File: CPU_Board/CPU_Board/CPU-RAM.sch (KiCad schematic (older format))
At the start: 65 parts

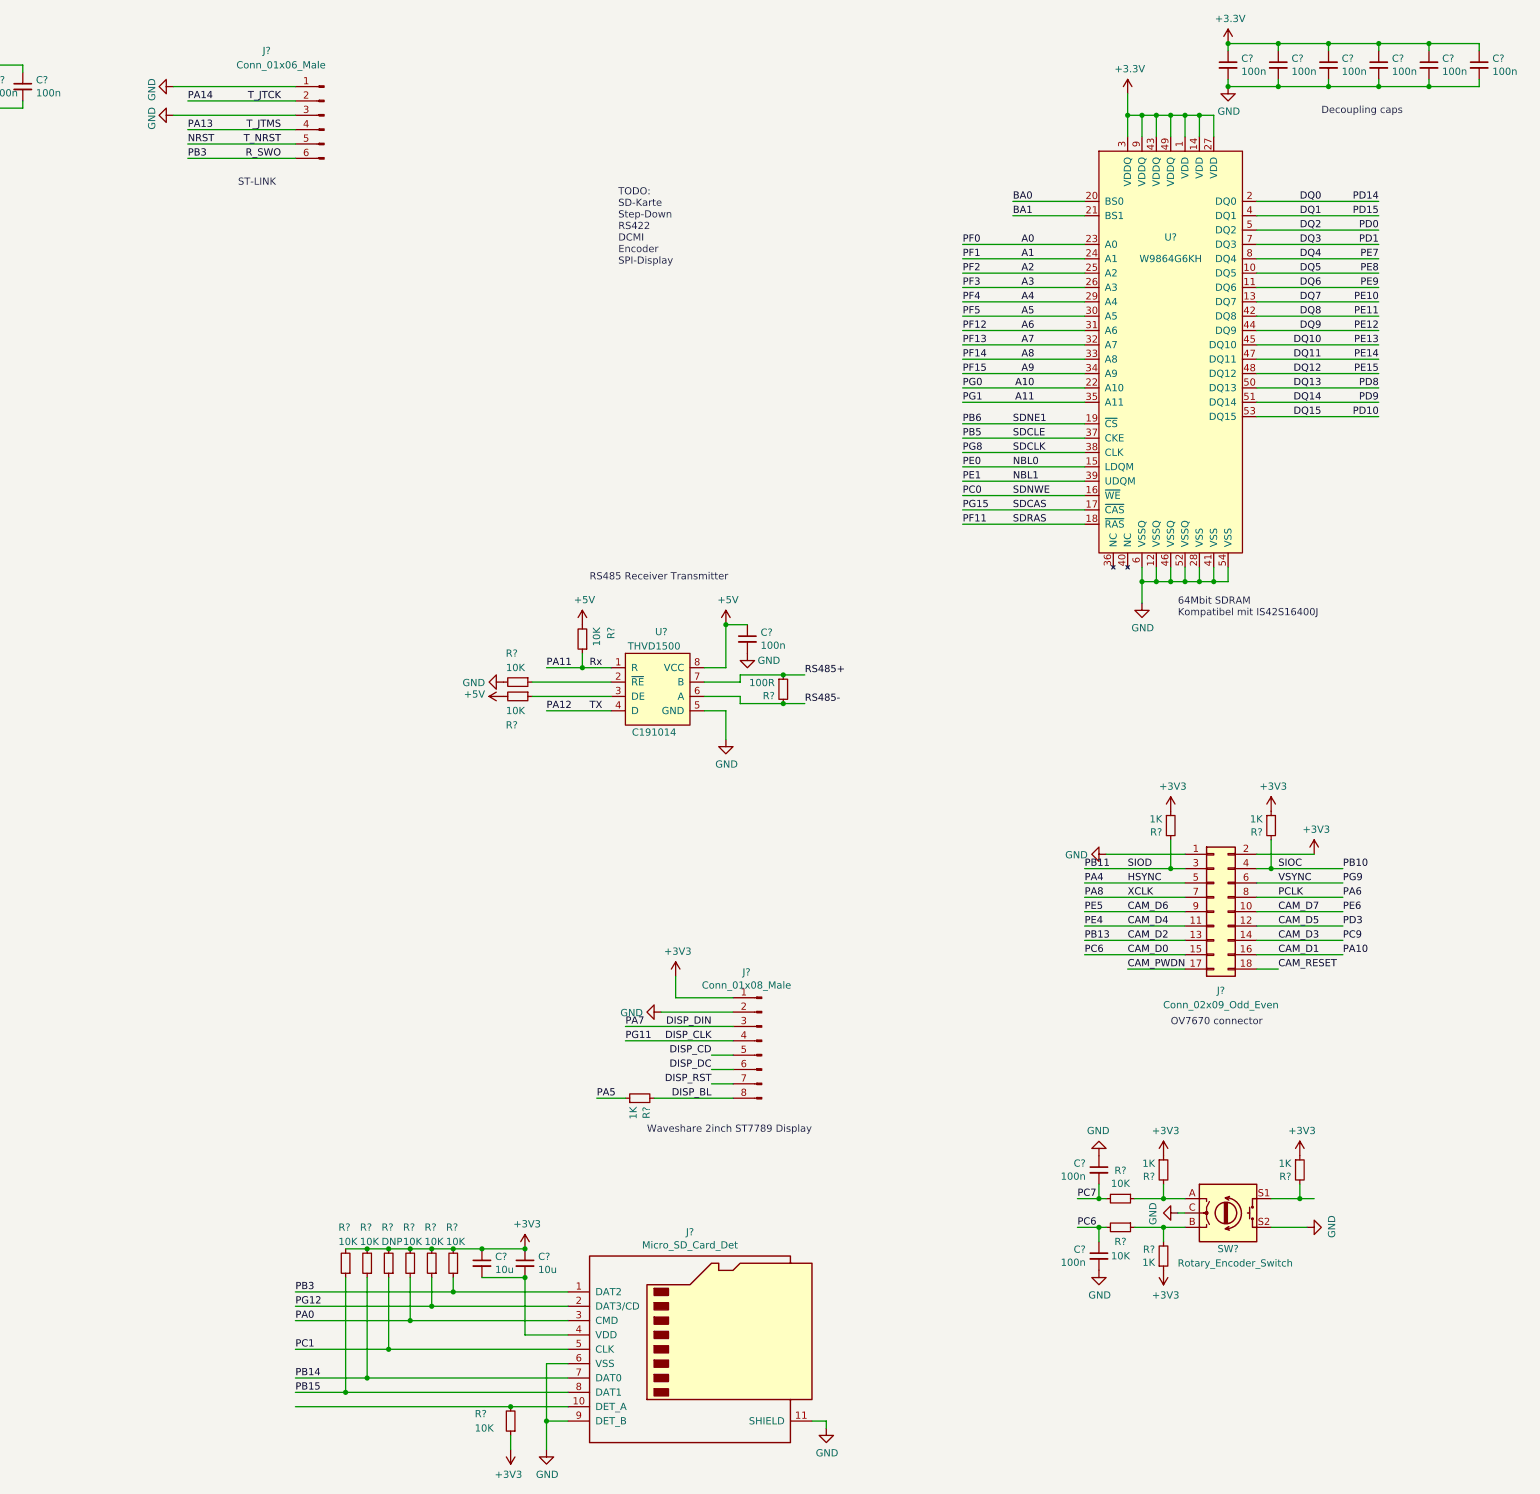
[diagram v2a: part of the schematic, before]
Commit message: sd card footprint, step down regler
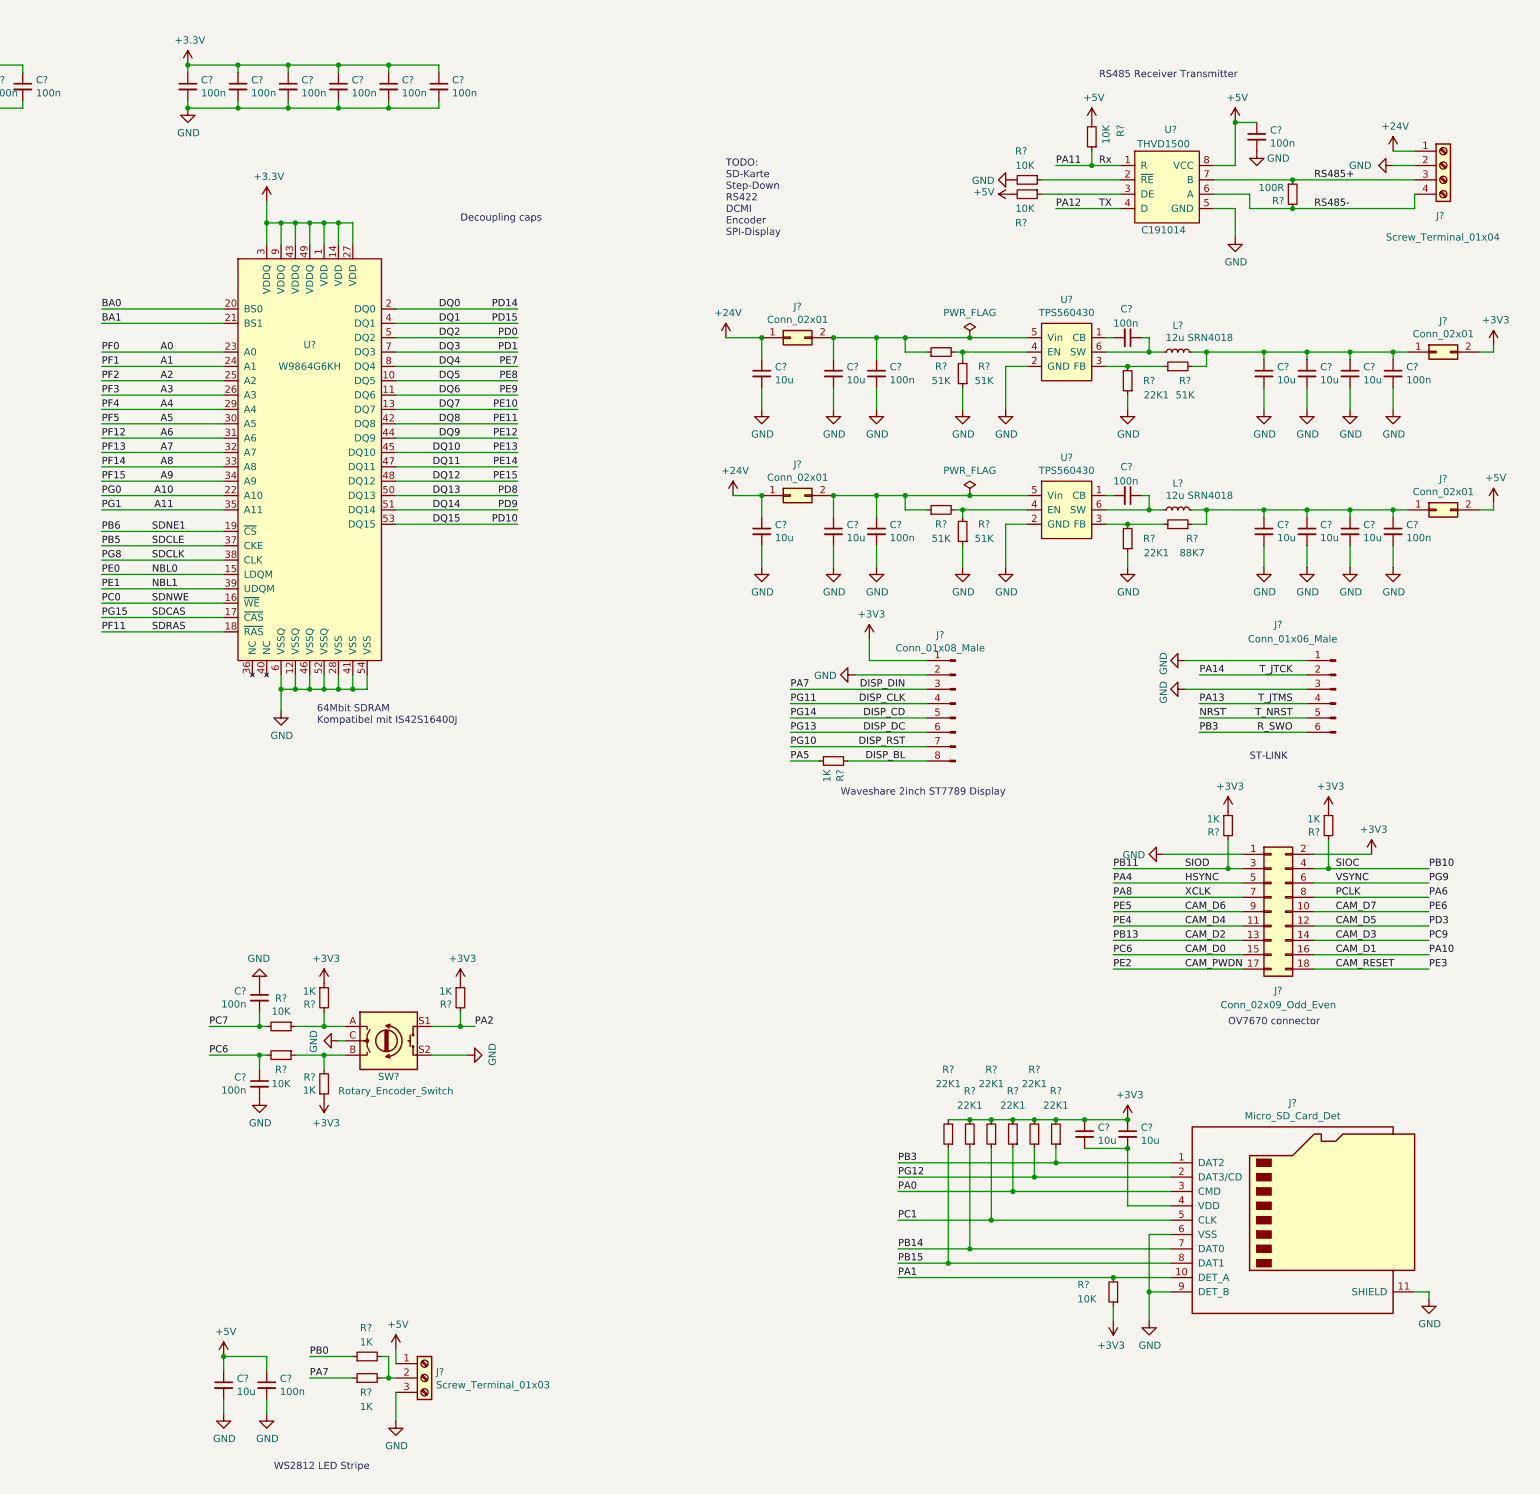
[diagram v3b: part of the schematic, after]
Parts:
- removed R? (x5): 10K, Resistor_SMD:R_0603_1608Metric, symbol Device:R_Small
- removed R?: DNP, Resistor_SMD:R_0603_1608Metric, symbol Device:R_Small
- added C? (x7): 100n, Capacitor_SMD:C_0603_1608Metric, symbol Device:C_Small
- added C? (x11): 10u, Capacitor_SMD:C_0603_1608Metric, symbol Device:C_Small
- added J? (x4): Conn_02x01, Connector_PinHeader_2.54mm:PinHeader_1x02_P2.54mm_Vertical, symbol Connector_Generic:Conn_02x01
- added J?: Screw_Terminal_01x04, TerminalBlock_RND:TerminalBlock_RND_205-00047_1x04_P5.00mm_Horizontal, symbol Connector:Screw_Terminal_01x04
- added J?: Screw_Terminal_01x03, TerminalBlock_RND:TerminalBlock_RND_205-00046_1x03_P5.00mm_Horizontal, symbol Connector:Screw_Terminal_01x03
- added L? (x2): 12u SRN4018, Inductor_SMD:L_Bourns-SRN4018, symbol Device:L_Small
- added R? (x5): 51K, Resistor_SMD:R_0603_1608Metric_Pad1.05x0.95mm_HandSolder, symbol Device:R_Small
- added R? (x8): 22K1, Resistor_SMD:R_0603_1608Metric_Pad1.05x0.95mm_HandSolder, symbol Device:R_Small
- added R?: 88K7, Resistor_SMD:R_0603_1608Metric_Pad1.05x0.95mm_HandSolder, symbol Device:R_Small
- added R? (x2): 1K, Resistor_SMD:R_0603_1608Metric, symbol Device:R_Small
- added U? (x2): TPS560430, symbol PorjectLibrary:TPS560430
- FB?: LCSC C285924 -> C513774
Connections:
- net PE2 is gone; now on net CAM_PWDN: U?.1 (PE2)
- net PE3 is gone; now on net CAM_RESET: U?.2 (PE3)
- net PG10 is gone; now on net DISP_RST: U?.125 (PG10)
- net PG13 is gone; now on net DISP_DC: U?.128 (PG13)
- net PG14 is gone; now on net DISP_CD: U?.129 (PG14)
- net +3V3: now also J?.2 (Pin_2), R?.2, R?.2, R?.2, R?.2, R?.2, R?.2
- net +5V: now also C?.1, C?.1, J?.1 (Pin_1), J?.2 (Pin_2)
- net DISP_DIN: now also R?.1
- net GND: now also C?.2, C?.2, C?.2, C?.2, C?.2, C?.2, C?.2, C?.2, C?.2, C?.2, C?.2, C?.2, C?.2, C?.2, C?.2, C?.2, J?.2 (Pin_2), J?.3 (Pin_3), R?.1, R?.1, R?.1, R?.1, U?.2 (GND), U?.2 (GND)
- net PA0: now also R?.1
- net PA1: now also J?.10 (DET_A), R?.2
- net PA2: now also R?.2, SW?.S1
- net PB0: now also R?.1
- net PB14: now also R?.1
- net PB15: now also R?.1
- net PB3: now also R?.1
- net PC1: now also R?.1
- net PG12: now also R?.1
- net RS485+: now also J?.3 (Pin_3)
- net RS485-: now also J?.4 (Pin_4)
- new net: C?.1, C?.1, C?.1, C?.1, J?.1 (Pin_1), L?.2, R?.2 (x2)
- new net: C?.1, C?.1, J?.2 (Pin_2), R?.1, U?.5 (Vin) (x2)
- new net: C?.1, L?.1, U?.6 (SW) (x2)
- new net: R?.1, R?.2, U?.3 (FB) (x2)
- new net: C?.2, U?.1 (CB) (x2)
- new net: R?.2, R?.2, U?.4 (EN) (x2)
- new net: J?.2 (Pin_2), R?.2, R?.2
- new net +24V: C?.1, C?.1, J?.1 (Pin_1), J?.1 (Pin_1), J?.1 (Pin_1)
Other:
- note added: "WS2812 LED Stripe"
- moved on the sheet: C?, J?, R?, SW?, U?
